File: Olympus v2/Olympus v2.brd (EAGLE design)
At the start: 203.2 x 152.4 mm, 170 parts, among them J1 HEADER_10P_0.05, Q1 BSS138, Q10 BSS138, Q11 BSS138, Q12 BSS138, Q2 BSS138, Q3 BSS138, Q4 BSS138, Q5 BSS138, Q6 BSS138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

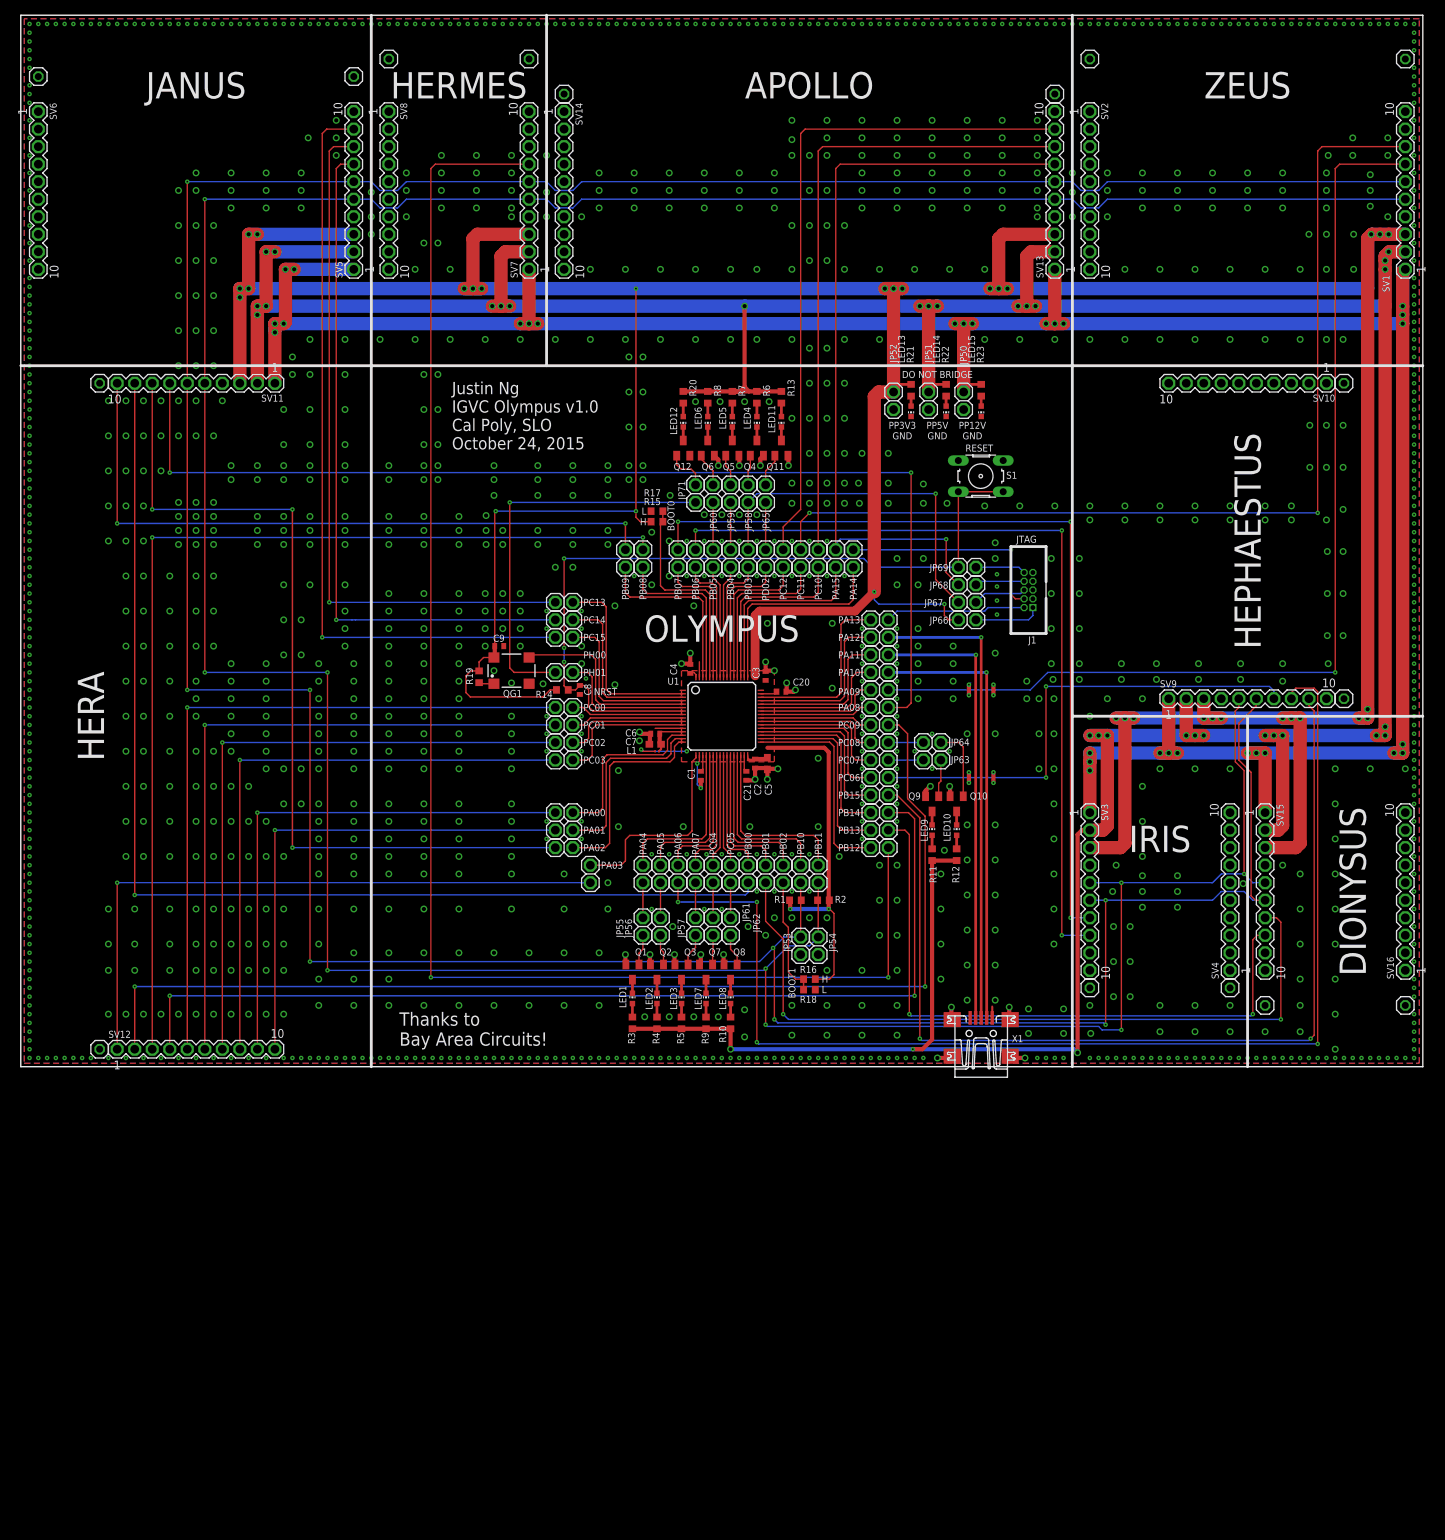
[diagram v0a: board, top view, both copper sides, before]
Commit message: I updated Olympus by changing the USB pins, the GPIO LEDS, and updated the Hermes, Hephaestus, and Iris pinouts and connections to the microcontroller.  I also added pull down resistors on theLEDS.
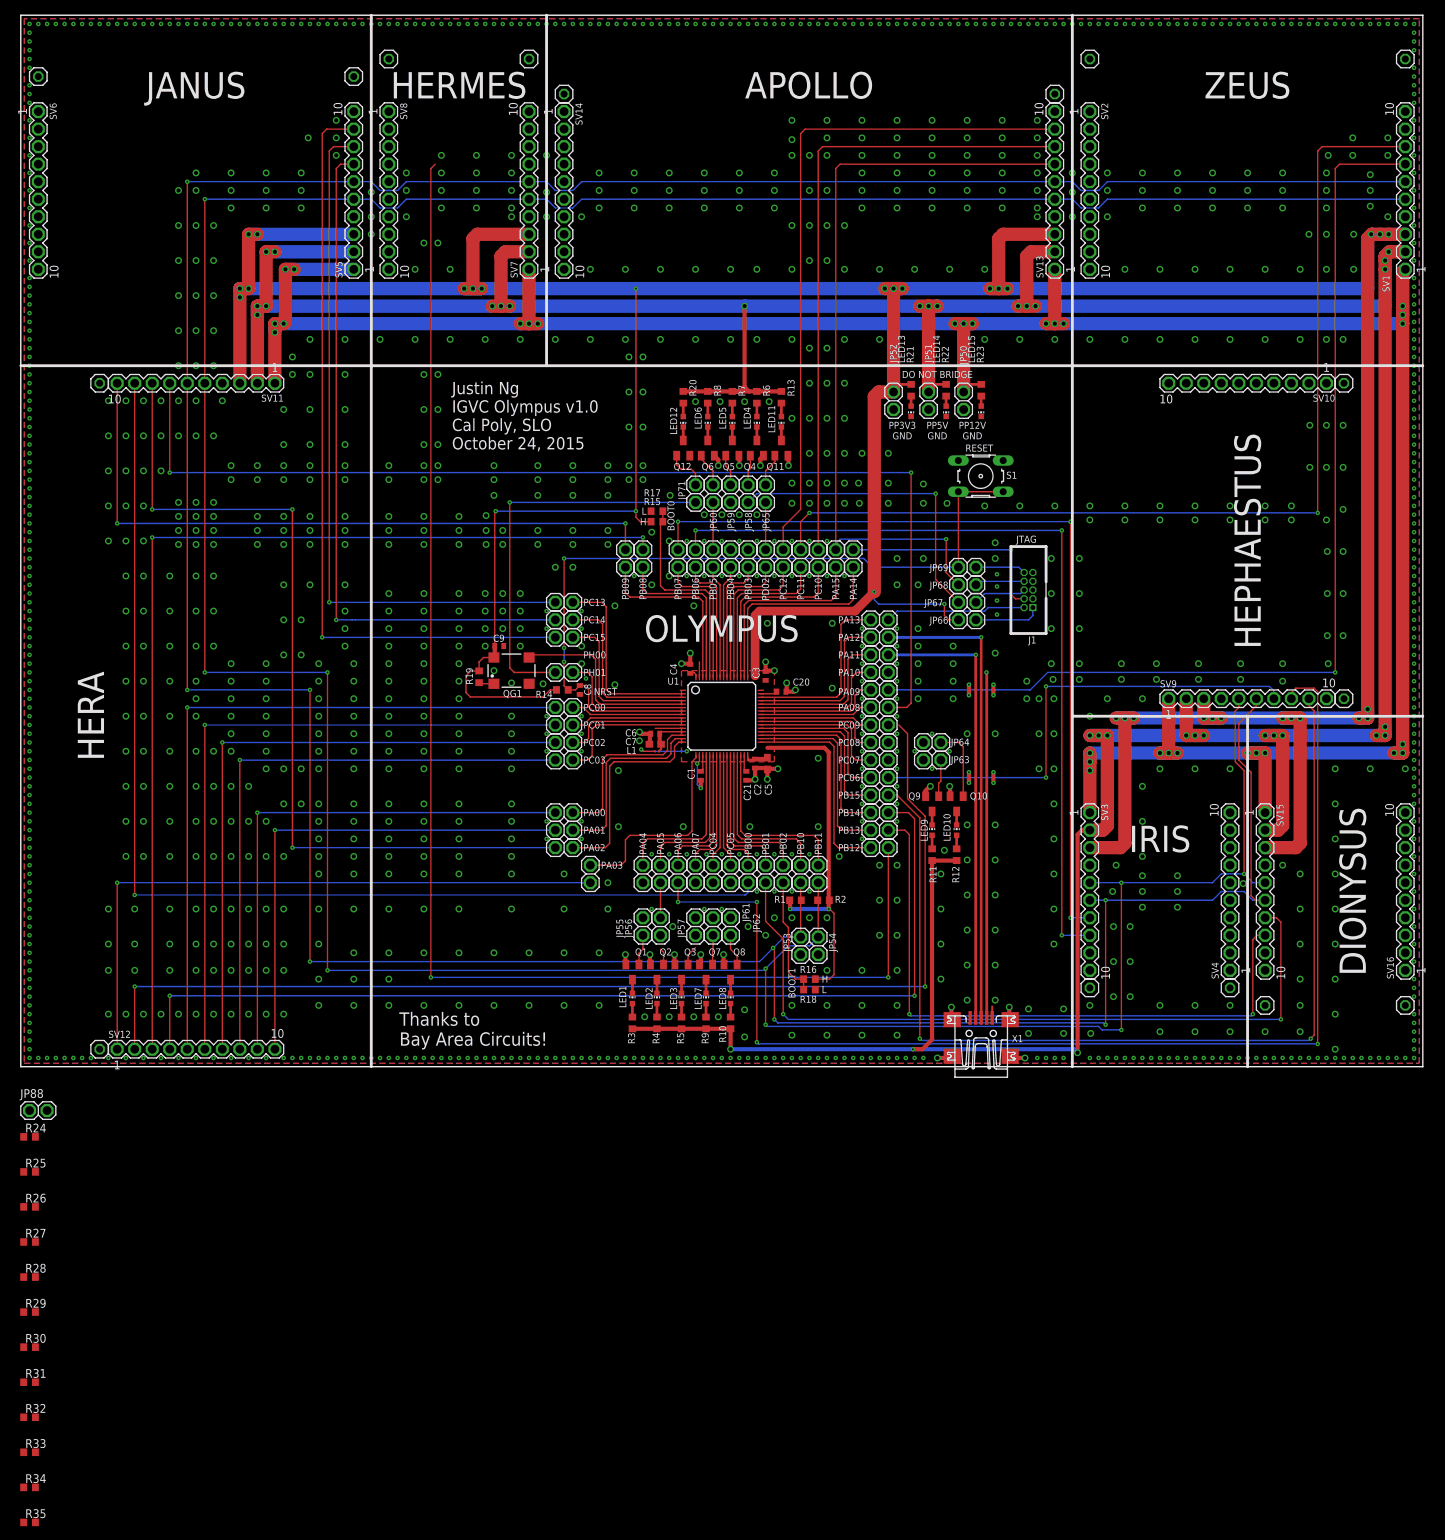
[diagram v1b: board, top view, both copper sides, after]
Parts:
- added JP88: (no value), pinhead:1X02
- added R24, R25, R26, R27, R28, R29, R30, R31, R32, R33, R34, R35: 10k, resistor:R0603
- R10, R11, R12, R13, R20, R3, R4, R5, R6, R7, R8, R9: value 100 -> 1k
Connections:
- new net ENABLE: SV7.7
- new net HEPHAESTUS_BRAKE_DIR: JP21.1
- new net HEPHAESTUS_BRAKE_DIR2: JP40.2
- new net HEPHAESTUS_BRAKE_FAULT: JP38.2
- new net HEPHAESTUS_DIR2: JP41.2
- new net HEPHAESTUS_PWM_BRAKE: JP8.1
- new net HEPHAESTUS_STEER_FAULT: JP37.2
- new net HERMES_PED_DETECT: JP5.1
- new net N$2: JP88.2
- new net OLYMPUS_DEBUG_LED: JP11.1
- new net OLYMPUS_JTAG_SWO: JP20.1
- new net TH_ADC: SV7.8
- net GND: now also R24.2, R25.2, R26.2, R27.2, R28.2, R29.2, R30.2, R31.2, R32.2, R33.2, R34.2, R35.2
- net HERA_HALL2: now also JP42.2
- net HERA_SONAR6: no longer JP42.2
- net HERMES_AUTOMAN: no longer SV7.7
- net LED10_G: now also R29.1
- net LED11_G: now also R30.1
- net LED12_G: now also R31.1
- net LED1_G: now also R24.1
- net LED2_G: now also R25.1
- net LED3_G: now also R26.1
- net LED4_G: now also R27.1
- net LED5_G: now also R32.1
- net LED6_G: now also R33.1
- net LED7_G: now also R34.1
- net LED8_G: now also R35.1
- net LED9_G: now also R28.1
- net MCU_BOOT0: now also JP88.1
- net OLYMPUS_GPIO1: no longer JP5.1
- net OLYMPUS_GPIO10: no longer JP41.2
- net OLYMPUS_GPIO3: no longer JP8.1
- net OLYMPUS_GPIO4: no longer JP20.1
- net OLYMPUS_GPIO5: no longer JP21.1
- net OLYMPUS_GPIO7: no longer JP37.2
- net OLYMPUS_GPIO8: no longer JP38.2
- net OLYMPUS_GPIO9: no longer JP40.2
- net OLYMPUS_USBID: no longer JP11.1
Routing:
- net OLYMPUS_USBID: track 64.3 -> 50.1 mm
- net HERMES_AUTOMAN: track 216.8 -> 203.2 mm
- net OLYMPUS_GPIO5: track 6.86 -> 0.00 mm
- net OLYMPUS_GPIO4: track 51.7 -> 44.8 mm
- net OLYMPUS_GPIO8: track 5.08 -> 0.00 mm
- net OLYMPUS_GPIO7: track 5.08 -> 0.00 mm
- net OLYMPUS_GPIO3: track 5.08 -> 0.00 mm
- net OLYMPUS_GPIO1: track 5.08 -> 0.00 mm
- net OLYMPUS_GPIO9: track 5.08 -> 0.00 mm
- net OLYMPUS_GPIO10: track 5.08 -> 0.00 mm
- net LED2_G: track 4.42 -> 2.39 mm
- net LED3_G: track 4.68 -> 2.90 mm
- net HERA_SONAR6: track 164.6 -> 163.1 mm
